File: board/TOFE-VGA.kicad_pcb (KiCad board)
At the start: 4 copper layers, 99 x 99 mm, 144 parts, among them P1 CONN_02X06, P601 3-RCA, U5V1 LP2985

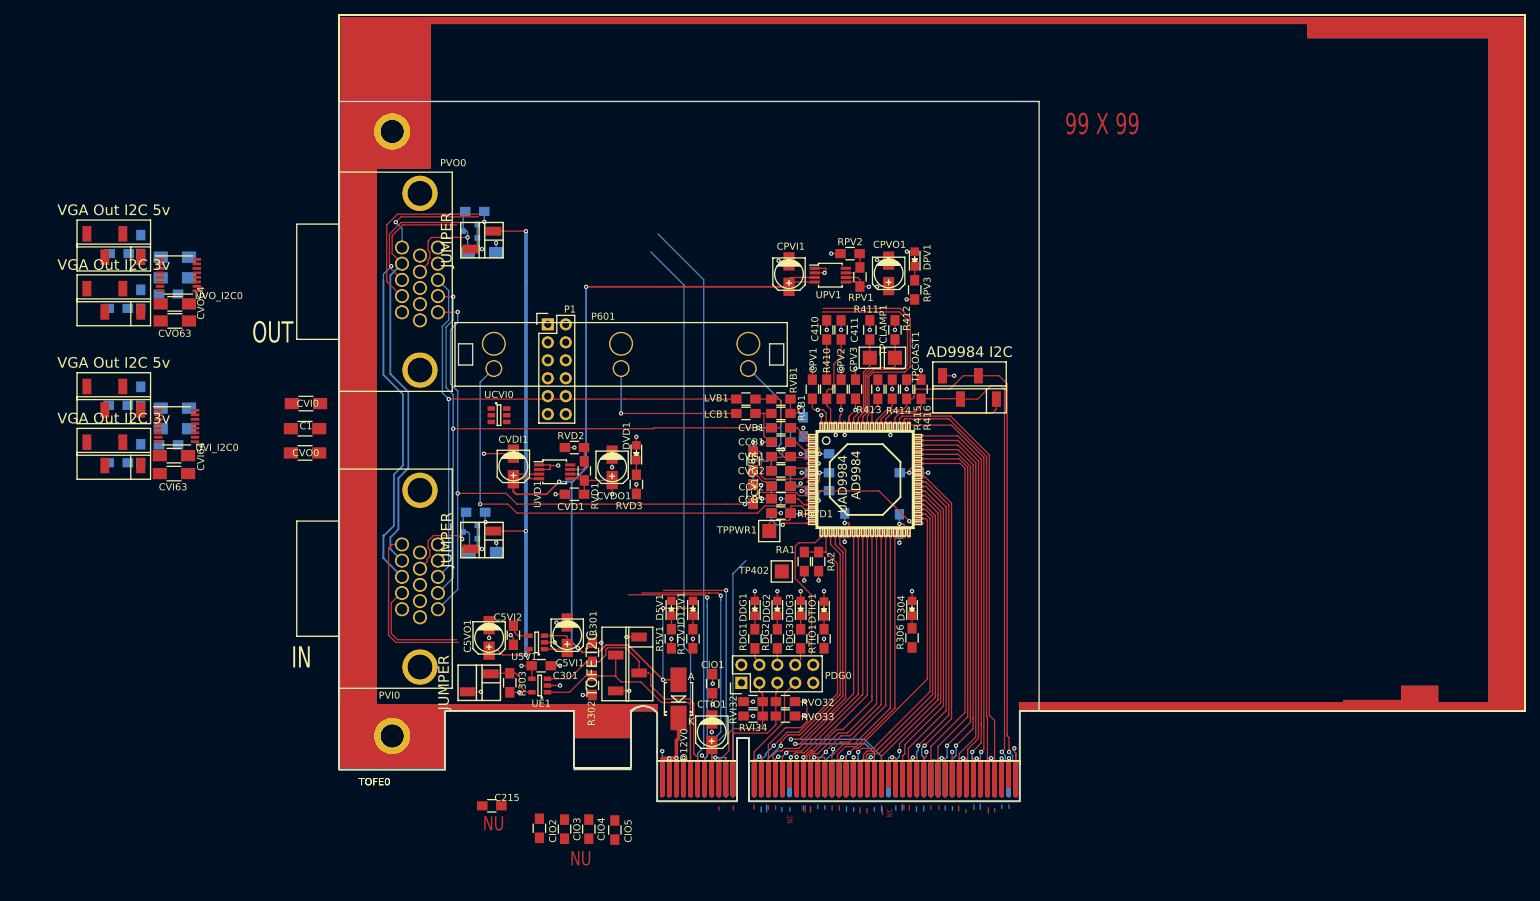
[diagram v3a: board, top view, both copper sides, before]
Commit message: Updating PCB from net list.
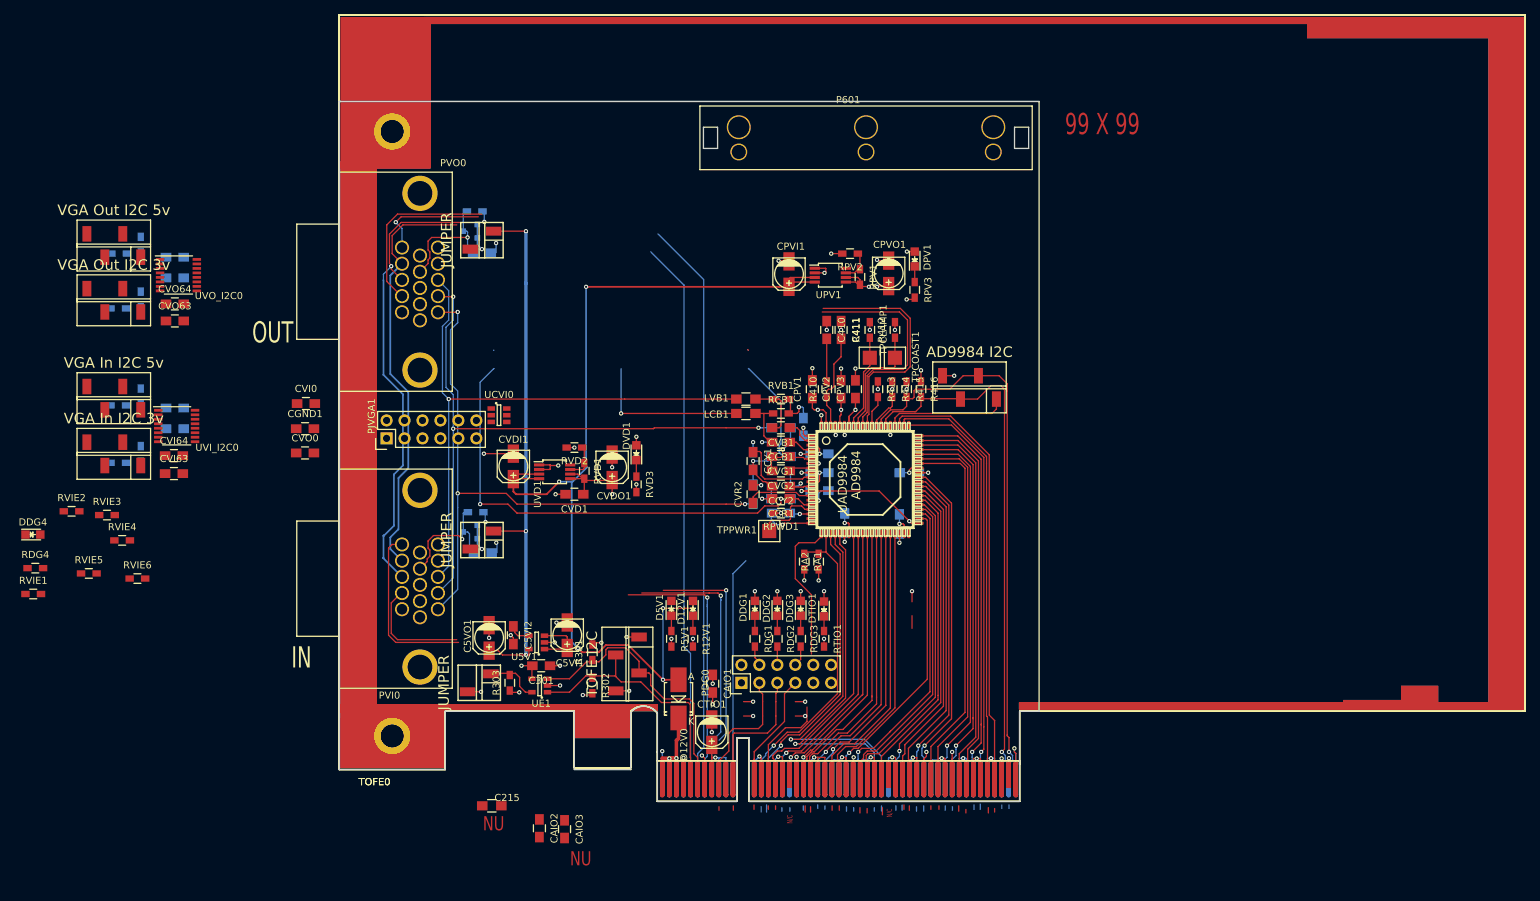
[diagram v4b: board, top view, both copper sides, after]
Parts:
- removed C1: C, Capacitors_SMD:C_1206_HandSoldering
- removed CI2C1, CI2C2, CIO1, CIO2, CIO3, CIO4, CIO5: 100n, Resistors_SMD:R_0805_HandSoldering
- removed D304: LED, LEDs:LED_0805
- removed R306: 68R, Resistors_SMD:R_0805_HandSoldering
- removed RVI32, RVI34, RVO32, RVO33: ?, Resistors_SMD:R_0805_HandSoldering
- removed TP402: TESTPOINT, 2MM-TESTPOINT:2MM-TESTPOINT
- added CAIO1: 100n, Capacitors_SMD:C_0805_HandSoldering, F.Cu at (115.0, 141.9)
- added CAIO2: 100n, Capacitors_SMD:C_0805_HandSoldering, F.Cu at (90.5, 162.3)
- added CAIO3: 100n, Capacitors_SMD:C_0805_HandSoldering, F.Cu at (94.1, 162.4)
- added CGND1: 100n, Capacitors_SMD:C_0805_HandSoldering, F.Cu at (57.4, 105.8)
- added DDG4: LED, LEDs:LED_0805, F.Cu at (18.9, 120.8)
- added RDG4: 68R, Resistors_SMD:R_0603_HandSoldering, F.Cu at (19.2, 125.5)
- added RVIE1: 0, Resistors_SMD:R_0603_HandSoldering, F.Cu at (18.9, 129.2)
- added RVIE2: 0, Resistors_SMD:R_0603_HandSoldering, F.Cu at (24.3, 117.5)
- added RVIE3: 0, Resistors_SMD:R_0603_HandSoldering, F.Cu at (29.4, 118.0)
- added RVIE4: 0, Resistors_SMD:R_0603_HandSoldering, F.Cu at (31.5, 121.6)
- added RVIE5: 0, Resistors_SMD:R_0603_HandSoldering, F.Cu at (26.8, 126.3)
- added RVIE6: 0, Resistors_SMD:R_0603_HandSoldering, F.Cu at (33.7, 127.0)
- C301, C410, C411, C5VI2, CCB1, CCR1, CCY1, CCY2, CPV1, CPV2, CPV3, CREF1, CVB1, CVD1, CVD2, CVD3, CVD4, CVD5, CVG1, CVG2, CVR2: footprint Resistors_SMD:R_0805_HandSoldering -> Capacitors_SMD:C_0805_HandSoldering
- C5VI1: value 1u -> 22u
- CVI0, CVO0: value C -> 100n; footprint Capacitors_SMD:C_1206_HandSoldering -> Capacitors_SMD:C_0805_HandSoldering
- CVI60, CVI61, CVI62, CVI63, CVI64, CVO60, CVO61, CVO62, CVO63, CVO64: value 100nF -> 100n; footprint Capacitors_SMD:C_1206_HandSoldering -> Capacitors_SMD:C_0805_HandSoldering
- PDG0: footprint Pin_Headers:Pin_Header_Straight_2x05 -> Pin_Headers:Pin_Header_Straight_2x06
- PVI_I2C3: value VGA Out I2C 3v -> VGA In I2C 3v
- PVI_I2C5: value VGA Out I2C 5v -> VGA In I2C 5v
- R12V1, R301, R302, R303, R410, R411, R412, R413, R414, R415, R416, R5V1, RA1, RA2, RCB1, RCR1, RCY1, RDG1, RDG2, RDG3, RPV1, RPV2, RPV3, RPWD1, RTIO1, RVB1, RVD1, RVD2, RVD3, RVG1, RVI30, RVI31, RVI50, RVI51, RVI60, RVO30, RVO31, RVO50, RVO51, RVO60, RVR1: footprint Resistors_SMD:R_0805_HandSoldering -> Resistors_SMD:R_0603_HandSoldering
- moved P601 46.2 mm to (136.7, 60.1)
- moved PJVGA1 27.9 mm to (68.9, 107.2), turned to 90 degrees
- renumbered P1 to PJVGA1
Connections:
- PAD_I2C0 pad 2: /TOFE-VGA/AD9984/SCL_AD9984 -> /SCL_AD99844
- PAD_I2C0 pad 3: /TOFE-VGA/AD9984/SDA_AD9984 -> /SDA_AD9984
- PDG0 pad 1: Net-(PDG0-Pad1) -> /TOFE-VGA/TOFE/IDDAT
- PDG0 pad 2: +3V3 -> Net-(PDG0-Pad2)
- PDG0 pad 3: /TOFE-VGA/TOFE/VGAIN_I2C_EN -> Net-(PDG0-Pad3)
- PDG0 pad 5: /TOFE-VGA/TOFE/VGAOUT_I2C_EN -> Net-(PDG0-Pad5)
- PDG0 pad 9: Net-(PDG0-Pad9) -> GND
- PJVGA1 pad 10: /TOFE-VGA/VGA/VGAIN_B -> /TOFE-VGA/VGA/VGAOUT_B
- PJVGA1 pad 6: /TOFE-VGA/VGA/VGAIN_R -> /TOFE-VGA/VGA/VGAOUT_R
- PJVGA1 pad 8: /TOFE-VGA/VGA/VGAIN_G -> /TOFE-VGA/VGA/VGAOUT_G
- PVI0 pad 10: GNDA -> GND
- PVI0 pad 12: /TOFE-VGA/VGA/VGAOUT5V_SDA -> /TOFE-VGA/VGA/VGAIN5V_SDA
- PVI0 pad 13: /TOFE-VGA/VGA/VGAOUT_HSYNC -> /TOFE-VGA/VGA/VGAIN_HSYNC
- PVI0 pad 14: /TOFE-VGA/VGA/VGAOUT_VSYNC -> /TOFE-VGA/VGA/VGAIN_VSYNC
- PVI0 pad 15: /TOFE-VGA/VGA/VGAOUT5V_SCL -> /TOFE-VGA/VGA/VGAIN5V_SCL
- PVI0 pad 5: GNDA -> GND
- PVI_I2C3 pad 2: /TOFE-VGA/VGA/VGAIN_SCL -> /VGAIN_SCL
- PVI_I2C3 pad 3: /TOFE-VGA/TOFE/VGAIN_SCL -> /VGAIN_SDA
- PVI_I2C5 pad 2: /TOFE-VGA/VGA/VGAOUT5V_SCL -> /TOFE-VGA/VGA/VGAIN5V_SCL
- PVI_I2C5 pad 3: /TOFE-VGA/VGA/VGAOUT5V_SDA -> /TOFE-VGA/VGA/VGAIN5V_SDA
- PVO0 pad 1: /TOFE-VGA/VGA/VGAIN_R -> /TOFE-VGA/VGA/VGAOUT_R
- PVO0 pad 10: GNDA -> GND
- PVO0 pad 2: /TOFE-VGA/VGA/VGAIN_G -> /TOFE-VGA/VGA/VGAOUT_G
- PVO0 pad 3: /TOFE-VGA/VGA/VGAIN_B -> /TOFE-VGA/VGA/VGAOUT_B
- PVO0 pad 5: GNDA -> GND
- PVO_I2C3 pad 2: /TOFE-VGA/VGA/VGAOUT_SCL -> /VGAOUT_SCL
- PVO_I2C3 pad 3: /TOFE-VGA/TOFE/VGAOUT_SCL -> /VGAOUT_SDA
- R415 pad 2: /TOFE-VGA/AD9984/SCL_AD9984 -> /SCL_AD99844
- R416 pad 2: /TOFE-VGA/AD9984/SDA_AD9984 -> /SDA_AD9984
- RA1 pad 1: /TOFE-VGA/AD9984/VSOUT -> /VSOUT
- RA2 pad 2: /TOFE-VGA/AD9984/VSOUT -> /VSOUT
- RDG1 pad 2: Net-(PDG0-Pad4) -> Net-(PDG0-Pad2)
- RDG2 pad 2: Net-(PDG0-Pad6) -> Net-(PDG0-Pad4)
- RDG3 pad 2: Net-(PDG0-Pad8) -> Net-(PDG0-Pad6)
- RPWD1 pad 1: /TOFE-VGA/AD9984/RST -> /RST
- RVI30 pad 2: /TOFE-VGA/TOFE/VGAIN_SCL -> /VGAIN_SDA
- RVI31 pad 2: /TOFE-VGA/VGA/VGAIN_SCL -> /VGAIN_SCL
- RVI50 pad 2: /TOFE-VGA/VGA/VGAOUT5V_SCL -> /TOFE-VGA/VGA/VGAIN5V_SCL
- RVI51 pad 2: /TOFE-VGA/VGA/VGAOUT5V_SDA -> /TOFE-VGA/VGA/VGAIN5V_SDA
- RVO30 pad 2: /TOFE-VGA/TOFE/VGAOUT_SCL -> /VGAOUT_SDA
- RVO31 pad 2: /TOFE-VGA/VGA/VGAOUT_SCL -> /VGAOUT_SCL
- TOFE0 pad A11: /TOFE-VGA/AD9984/RST -> /RST
- TOFE0 pad A13: /TOFE-VGA/AD9984/VSOUT -> /VSOUT
- TOFE0 pad A14: /TOFE-VGA/AD9984/HSOUT -> /HSOUT
- TOFE0 pad A29: /TOFE-VGA/AD9984/DATACK -> /DATACK
- TOFE0 pad A30: /TOFE-VGA/AD9984/SOGOUT -> /SOGOUT
- TOFE0 pad A47: /TOFE-VGA/AD9984/SDA_AD9984 -> /SDA_AD9984
- TOFE0 pad A48: /TOFE-VGA/AD9984/SCL_AD9984 -> /SCL_AD99844
- TOFE0 pad A5: /TOFE-VGA/VGA/VGAOUT_SCL -> /VGAOUT_SCL
- TOFE0 pad A6: /TOFE-VGA/TOFE/VGAOUT_SCL -> /VGAOUT_SDA
- TOFE0 pad A7: /TOFE-VGA/VGA/VGAIN_SCL -> /VGAIN_SCL
- TOFE0 pad A8: /TOFE-VGA/TOFE/VGAIN_SCL -> /VGAIN_SDA
- TOFE0 pad B11: /TOFE-VGA/TOFE/VGAOUT_I2C_EN -> Net-(PDG0-Pad5)
- TOFE0 pad B14: /TOFE-VGA/AD9984/FIELD -> /FIELD
- TOFE0 pad B9: /TOFE-VGA/TOFE/VGAIN_I2C_EN -> Net-(PDG0-Pad3)
- TPPWR1 pad 1: /TOFE-VGA/AD9984/RST -> /RST
- UAD9984 pad 17: /TOFE-VGA/AD9984/RST -> /RST
- UAD9984 pad 21: /TOFE-VGA/AD9984/FIELD -> /FIELD
- UAD9984 pad 22: /TOFE-VGA/AD9984/VSOUT -> /VSOUT
- UAD9984 pad 23: /TOFE-VGA/AD9984/HSOUT -> /HSOUT
- UAD9984 pad 24: /TOFE-VGA/AD9984/SOGOUT -> /SOGOUT
- UAD9984 pad 25: /TOFE-VGA/AD9984/DATACK -> /DATACK
- UAD9984 pad 66: /TOFE-VGA/AD9984/SDA_AD9984 -> /SDA_AD9984
- UAD9984 pad 67: /TOFE-VGA/AD9984/SCL_AD9984 -> /SCL_AD99844
- UVI_I2C0 pad 10: /TOFE-VGA/VGA/VGAIN_SCL -> /VGAIN_SCL
- UVI_I2C0 pad 11: /TOFE-VGA/TOFE/VGAIN_SCL -> /VGAIN_SDA
- UVI_I2C0 pad 12: /TOFE-VGA/VGA/VGAOUT5V_SDA -> /TOFE-VGA/VGA/VGAIN5V_SDA
- UVI_I2C0 pad 13: /TOFE-VGA/VGA/VGAIN_VSYNC -> Net-(RVIE1-Pad1)
- UVI_I2C0 pad 14: /TOFE-VGA/VGA/VGAOUT_VSYNC -> Net-(RVIE5-Pad2)
- UVI_I2C0 pad 15: /TOFE-VGA/VGA/VGAIN_HSYNC -> Net-(RVIE2-Pad1)
- UVI_I2C0 pad 16: /TOFE-VGA/VGA/VGAOUT_HSYNC -> Net-(RVIE6-Pad2)
- UVI_I2C0 pad 9: /TOFE-VGA/VGA/VGAOUT5V_SCL -> /TOFE-VGA/VGA/VGAIN5V_SCL
- UVO_I2C0 pad 10: /TOFE-VGA/VGA/VGAOUT_SCL -> /VGAOUT_SCL
- UVO_I2C0 pad 11: /TOFE-VGA/TOFE/VGAOUT_SCL -> /VGAOUT_SDA
- UVO_I2C0 pad 3: /TOFE-VGA/VGA/VGAIN_B -> /TOFE-VGA/VGA/VGAOUT_B
- UVO_I2C0 pad 4: /TOFE-VGA/VGA/VGAIN_G -> /TOFE-VGA/VGA/VGAOUT_G
- UVO_I2C0 pad 5: /TOFE-VGA/VGA/VGAIN_R -> /TOFE-VGA/VGA/VGAOUT_R
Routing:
- net /VGAOUT_SDA: track 0.00 -> 80.1 mm
- net /TOFE-VGA/TOFE/VGAOUT_SCL: track 80.1 -> 0.00 mm
- net /VGAOUT_SCL: track 0.00 -> 76.9 mm
- net /TOFE-VGA/VGA/VGAOUT_SCL: track 76.9 -> 0.00 mm
- net /TOFE-VGA/AD9984/SDA_AD9984: track 76.4 -> 0.00 mm, vias 1 -> 0
- net /SDA_AD9984: track 0.00 -> 76.4 mm, vias 0 -> 1
- net /TOFE-VGA/AD9984/SOGOUT: track 50.3 -> 0.00 mm, vias 1 -> 0
- net /SOGOUT: track 0.00 -> 50.3 mm, vias 0 -> 1
- net /TOFE-VGA/AD9984/DATACK: track 48.7 -> 0.00 mm, vias 1 -> 0
- net /DATACK: track 0.00 -> 48.7 mm, vias 0 -> 1
- net /TOFE-VGA/VGA/VGAOUT_HSYNC: track 65.7 -> 19.4 mm
- net /TOFE-VGA/VGA/VGAIN_HSYNC: track 33.1 -> 79.4 mm
- net /TOFE-VGA/AD9984/RST: track 40.8 -> 0.00 mm
- net /RST: track 0.00 -> 40.8 mm
- net /TOFE-VGA/AD9984/HSOUT: track 40.4 -> 0.00 mm, vias 1 -> 0
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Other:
- board text added: "P601 must be on board edge"
